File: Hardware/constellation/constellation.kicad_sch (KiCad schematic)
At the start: 0 parts

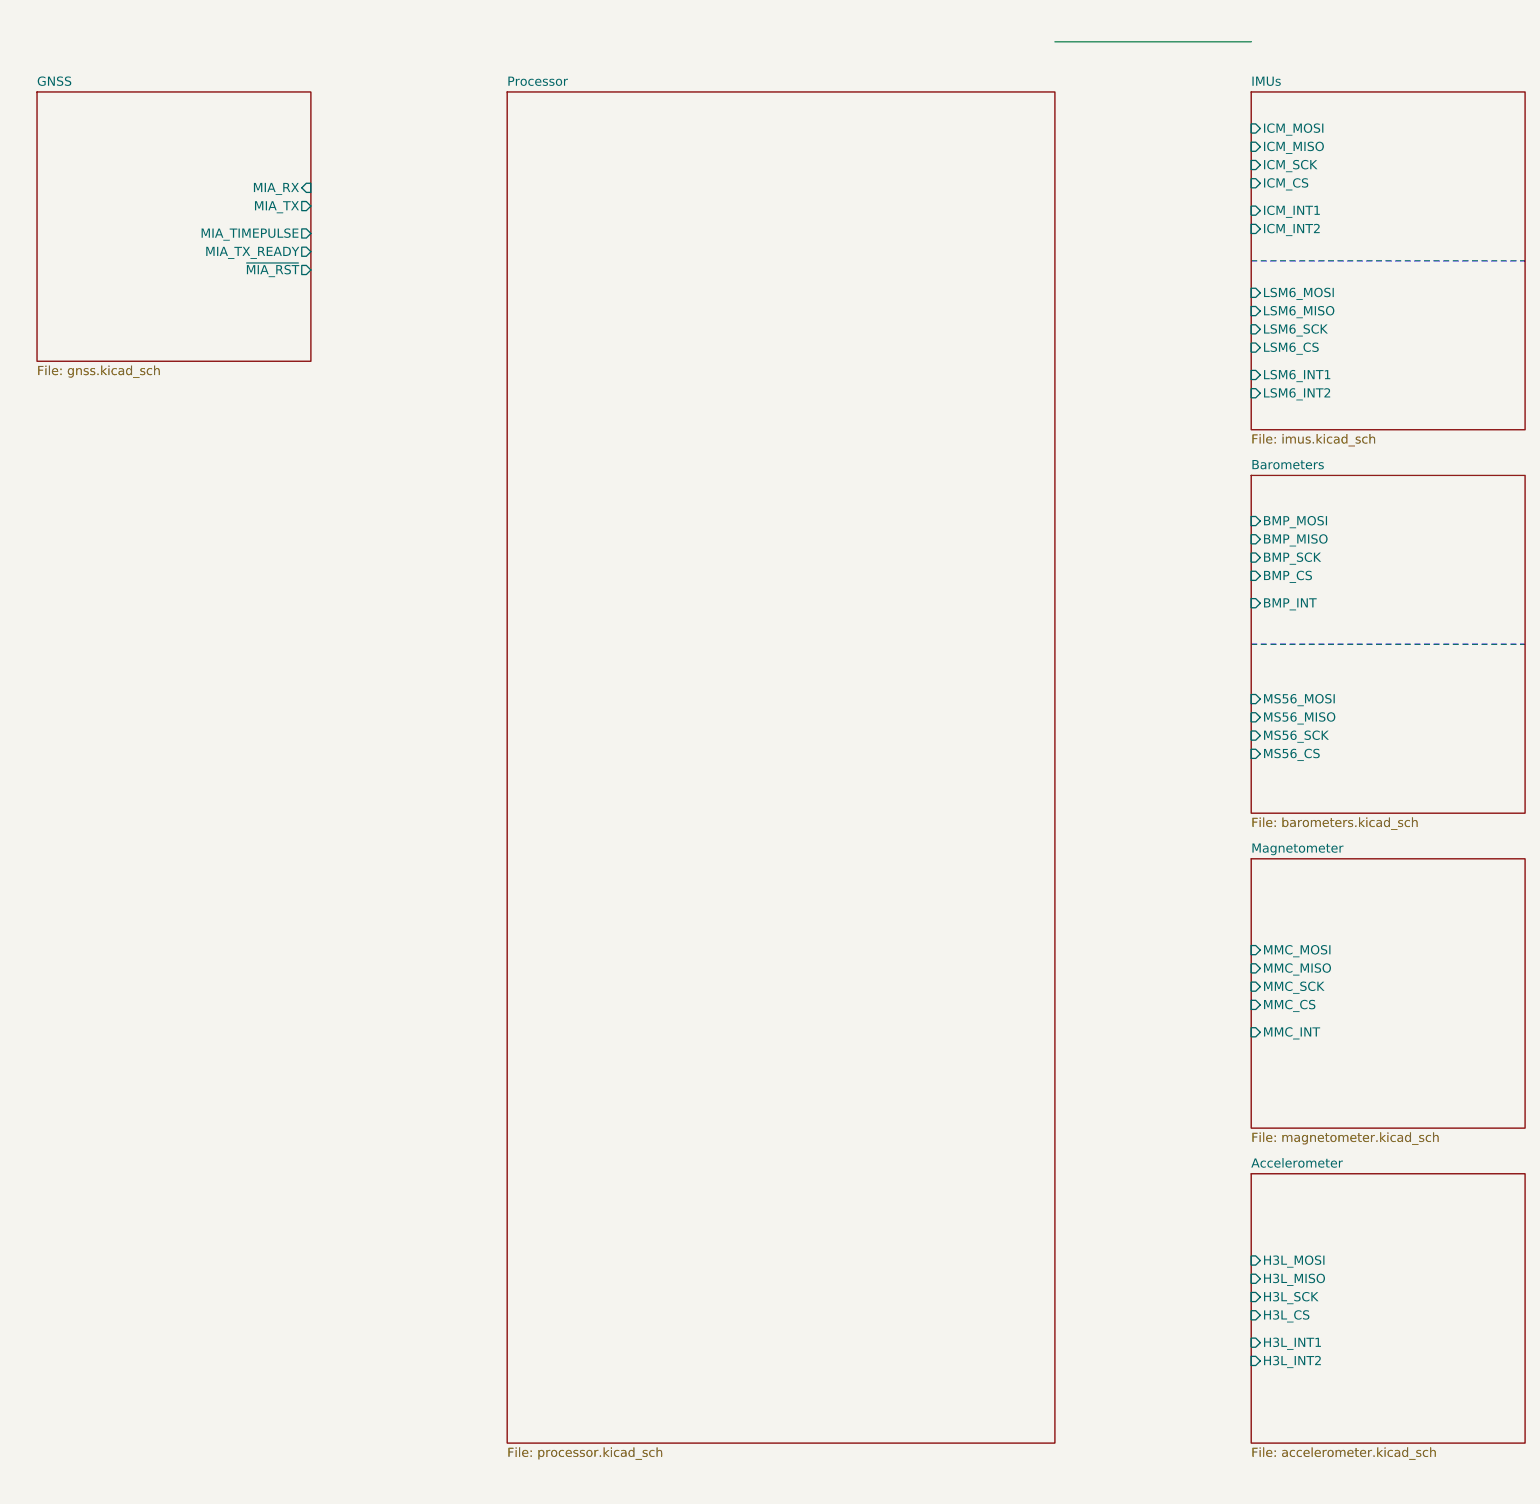
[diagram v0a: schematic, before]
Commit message: actually fix the magnetometer issue, start work on lora
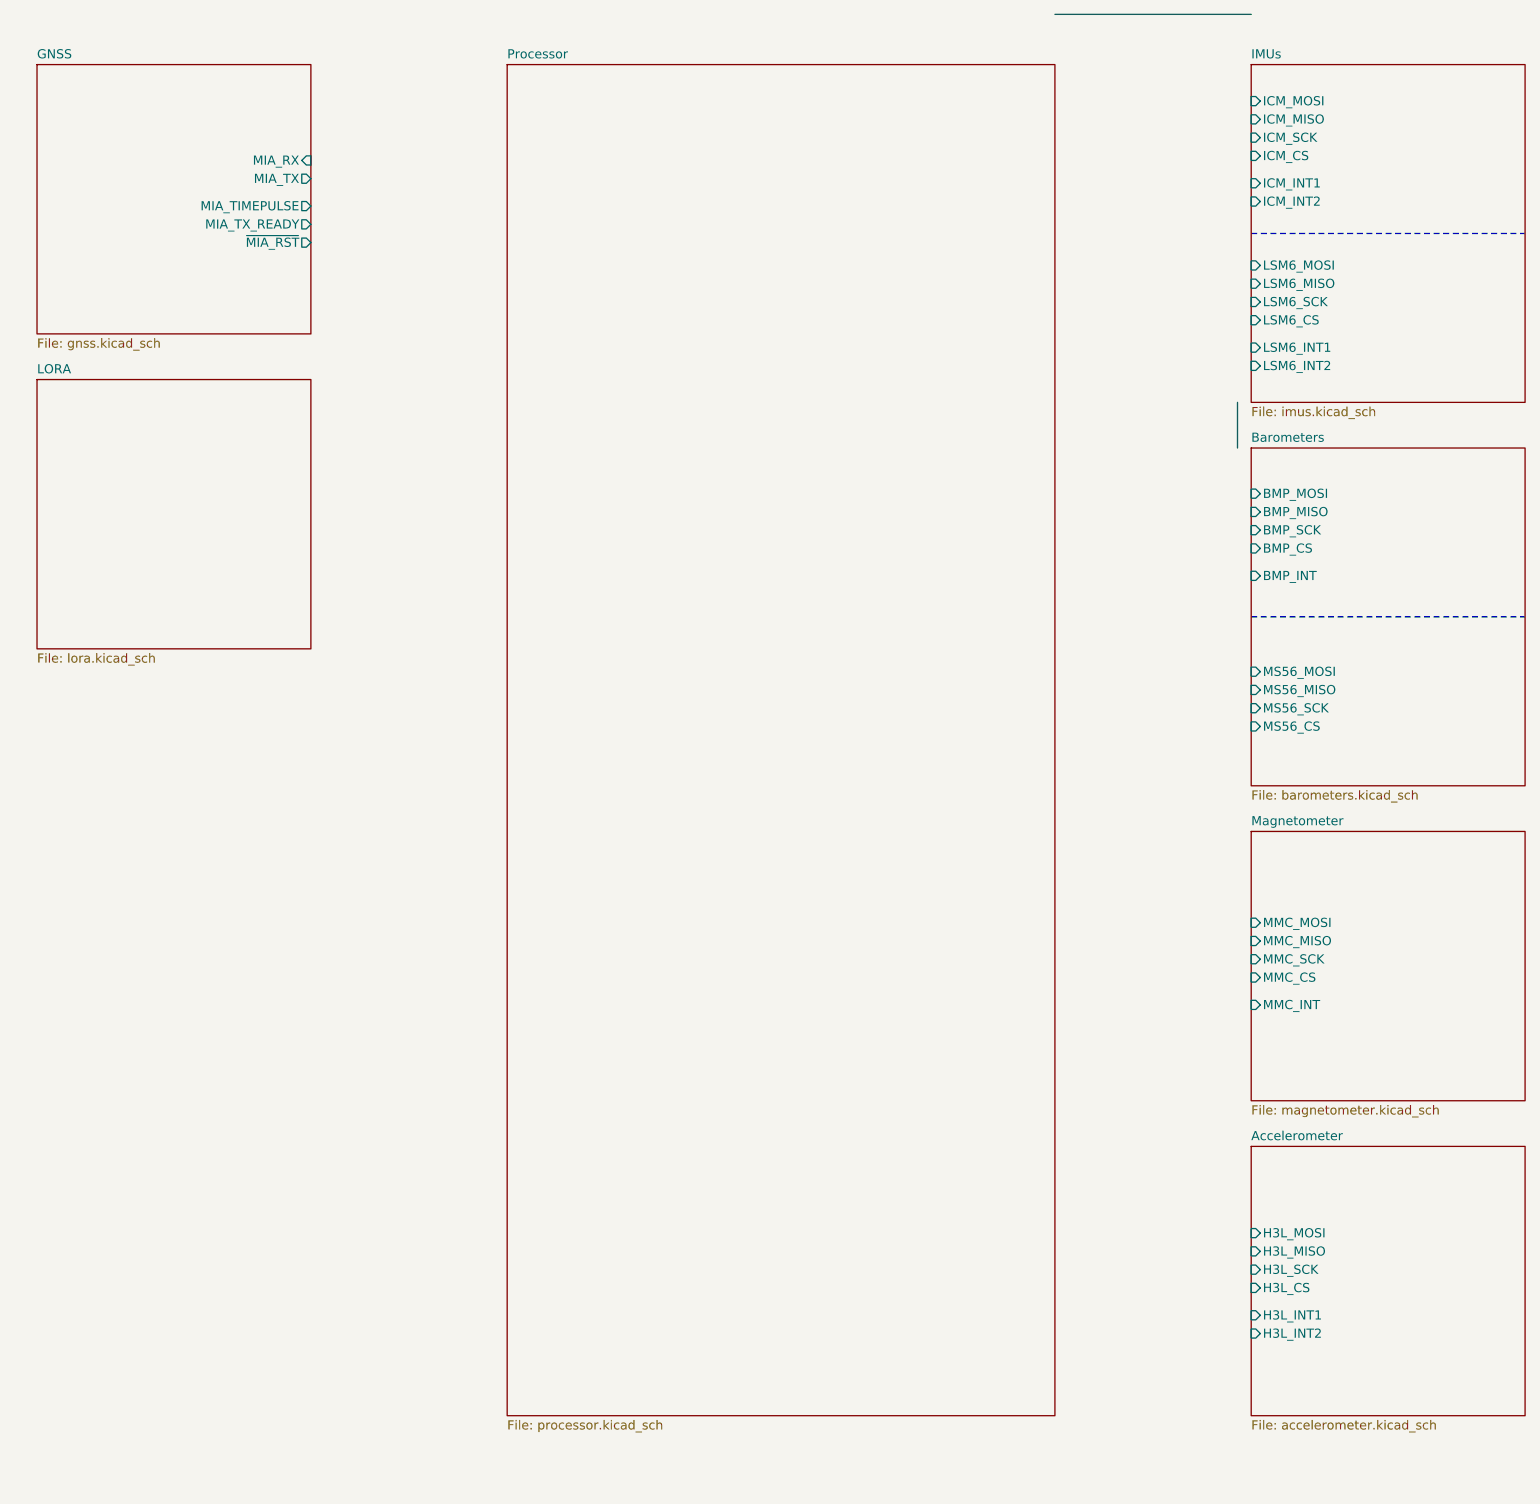
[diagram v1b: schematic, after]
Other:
- added sheet LORA (lora.kicad_sch)

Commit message: add pyro stuff, start system power
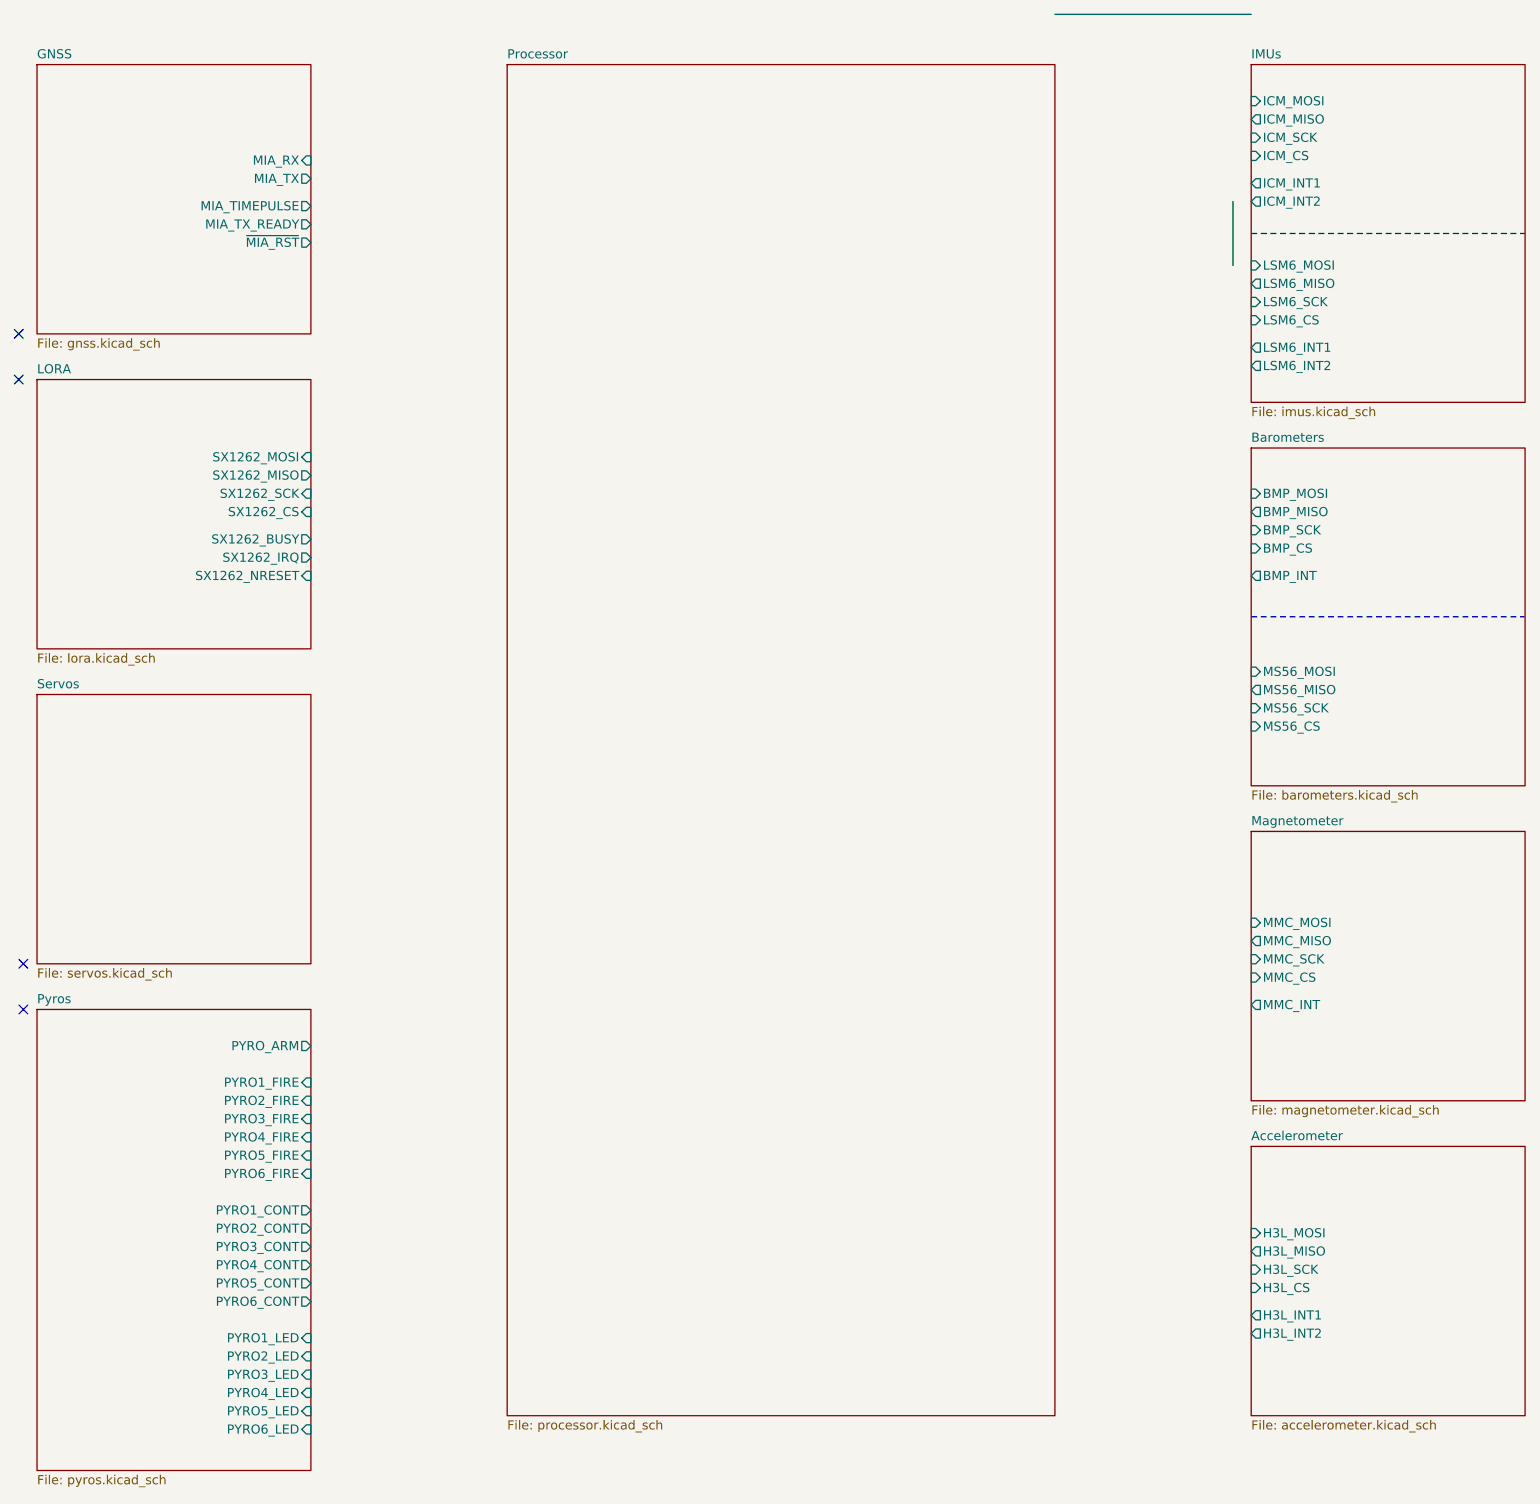
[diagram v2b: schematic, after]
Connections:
- no-connect marks 0 -> 4
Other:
- added sheet Pyros (pyros.kicad_sch)
- added sheet Servos (servos.kicad_sch)
- sheet LORA ports: added SX1262_BUSY, SX1262_CS, SX1262_IRQ, SX1262_MISO, SX1262_MOSI, SX1262_NRESET, SX1262_SCK; removed none
